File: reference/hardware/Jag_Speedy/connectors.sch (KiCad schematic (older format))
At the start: 8 parts, among them J1 Inputs, J2 Ouputs01, J3 Outputs02, J4 Power, J5 Bluetooth, J7 Canbus, U5 SN65HVD230

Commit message: Connector update
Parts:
- removed J1: Inputs, Connector_PinHeader_1.00mm:PinHeader_2x12_P1.00mm_Horizontal, symbol Connector_Generic:Conn_01x24
- removed J2: Ouputs01, Connector_PinHeader_1.00mm:PinHeader_2x07_P1.00mm_Horizontal, symbol Connector_Generic:Conn_01x14
- removed J3: Outputs02, Connector_PinHeader_1.00mm:PinHeader_2x05_P1.00mm_Horizontal, symbol Connector_Generic:Conn_01x10
- removed J4: Power, Connector_PinHeader_1.00mm:PinHeader_1x05_P1.00mm_Horizontal, symbol Connector_Generic:Conn_01x05
- removed J5: Bluetooth, Connector_PinHeader_1.00mm:PinHeader_1x06_P1.00mm_Horizontal, symbol Connector_Generic:Conn_01x06
- removed J7: Canbus, Connector_PinHeader_1.00mm:PinHeader_1x06_P1.00mm_Horizontal, symbol Connector_Generic:Conn_01x02
- added J1: 776087-1, 776087-1:7760871, symbol 776087-1:776087-1
- added J2: 776163-1, 776163-1:776163-1, symbol 776163-1:776163-1
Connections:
- net 12VRaw: now also J1.14
- net 3V3: now also J1.20, J2.1
- net 5V: now also J1.11, J1.19, J2.18
- net BluetoothRx: now also J1.22
- net BluetoothTx: now also J1.23
- net BoostPWM-OUT: now also J1.1
- net CCPump-OUT: now also J1.2
- net CLTSensor: now also J2.8
- net CamSensor+: now also J2.16
- net CamSensor-: now also J2.17
- net ClutchSwitch: now also J2.21
- net CrankSensor+: now also J2.14
- net CrankSensor-: now also J2.15
- net Fan-OUT: now also J1.5
- net FlexFuelSensor: now also J2.2
- net FuelPressureSensor: now also J2.19
- net FuelPump-OUT: now also J1.4
- net GND: now also J1.10, J1.17, J1.18, J1.21, J1.3, J1.9, J2.11, J2.12, J2.13, J2.22, J2.3, J2.35, J2.5, J2.7, J2.9
- net IATSensor: now also J2.6
- net Idle02-OUT: now also J1.7
- net IdlePWM-OUT: now also J1.6
- net Ign01-OUT: now also J2.29
- net Ign02-OUT: now also J2.30
- net Ign03-OUT: now also J2.31
- net Ign04-OUT: now also J2.32
- net Ign05-OUT: now also J2.33
- net Ign06-OUT: now also J2.34
- net Inj01-OUT: now also J2.23
- net Inj02-OUT: now also J2.24
- net Inj03-OUT: now also J2.25
- net Inj04-OUT: now also J2.26
- net Inj05-OUT: now also J2.27
- net Inj06-OUT: now also J2.28
- net O2Sensor: now also J2.10
- net OilPressureSensor: now also J2.20
- net TPSSensor: now also J2.4
- net Tacho-OUT: now also J1.8
- net CANL: now reaches U5.6 (CANL)
- net CANL: now also J1.16
- net CANH: now reaches U5.7 (CANH)
- net CANH: now also J1.15
- no-connect marks 3 -> 5
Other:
- moved on the sheet: R92, U5

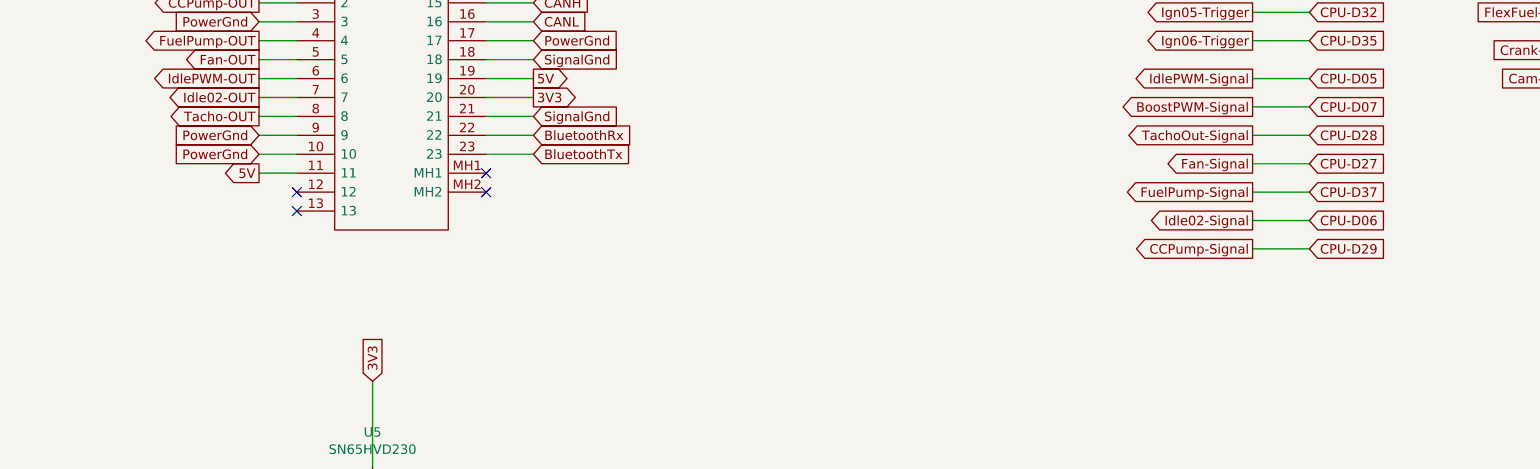
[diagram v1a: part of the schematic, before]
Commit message: Added Water Pump PWM
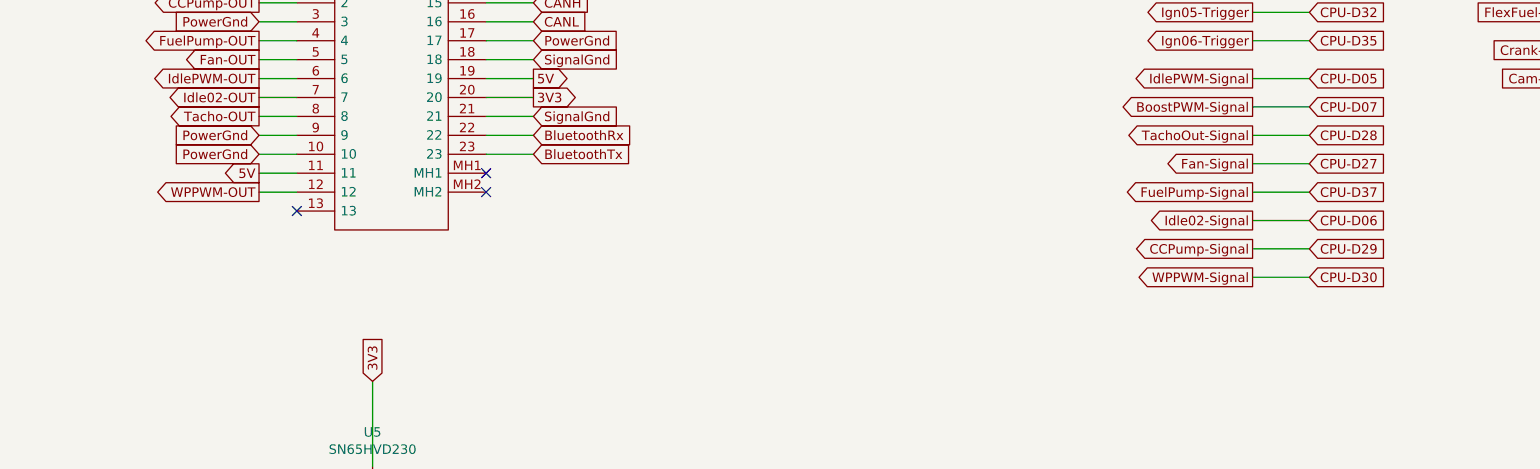
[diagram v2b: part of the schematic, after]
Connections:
- net WPPWM-OUT: now reaches J1.12
- no-connect marks 5 -> 4
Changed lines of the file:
@@
 	1750 4150 1950 4150
 NoConn ~ 1950 4350
-NoConn ~ 1950 4250
 NoConn ~ 2950 4250
 NoConn ~ 2950 4150
+Text GLabel 1750 4250 0    50   Output ~ 0
+WPPWM-OUT
+Wire Wire Line
+	1750 4250 1950 4250
+Text GLabel 7000 4700 0    50   Output ~ 0
+WPPWM-Signal
+Text GLabel 7300 4700 2    50   Input ~ 0
+CPU-D30
+Wire Wire Line
+	7300 4700 7000 4700
 $EndSCHEMATC

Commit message: EGR Input
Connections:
- net GND: no longer J2.12
- new net EGRSensor: J2.12
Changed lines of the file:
@@
 Wire Wire Line
 	2050 2050 1050 2050
-Wire Wire Line
-	1050 2050 1050 1950
 Text GLabel 3200 3650 2    50   Output ~ 0
 5V
@@
 Text GLabel 9250 2950 2    50   Output ~ 0
 CPU-A11
-Text GLabel 8800 3300 0    50   Input ~ 0
-FlexFuel-Signal
-Text GLabel 8800 3150 0    50   Input ~ 0
-ClutchIn-Signal
-Text GLabel 9250 3150 2    50   Output ~ 0
-CPU-D24
-Text GLabel 9250 3300 2    50   Output ~ 0
-CPU-D25
 Wire Wire Line
 	8800 1900 9250 1900
@@
 Wire Wire Line
 	9250 2950 8800 2950
-Wire Wire Line
-	8800 3150 9250 3150
-Wire Wire Line
-	9250 3300 8800 3300
 Text GLabel 8800 1750 0    50   Input ~ 0
 IAT-Signal-3V3
@@
 Wire Wire Line
 	8800 1750 9250 1750
-Text GLabel 8800 3500 0    50   Input ~ 0
-Crank-Signal
-Text GLabel 8800 3650 0    50   Input ~ 0
-Cam-Signal
-Text GLabel 9250 3650 2    50   Output ~ 0
-CPU-D36
-Text GLabel 9250 3500 2    50   Output ~ 0
-CPU-D23
-Wire Wire Line
-	8800 3650 9250 3650
-Wire Wire Line
-	9250 3500 8800 3500
 $Comp
 L Interface_CAN_LIN:SN65HVD230 U?
@@
 OilPressureSensor
 Wire Wire Line
-	2050 1950 1050 1950
-Connection ~ 1050 1950
-Wire Wire Line
-	1050 1950 1050 1850
-Wire Wire Line
 	3100 850  2950 850
 Wire Wire Line
@@
 Wire Wire Line
 	7300 4700 7000 4700
+Wire Wire Line
+	1050 1850 1050 2050
+Text GLabel 1900 1950 0    50   Input ~ 0
+EGRSensor
+Text GLabel 8800 3100 0    50   Input ~ 0
+EGR-Signal-3V3
+Text GLabel 9250 3100 2    50   Output ~ 0
+CPU-A6
+Wire Wire Line
+	9250 3100 8800 3100
+Wire Wire Line
+	9250 3700 8800 3700
+Wire Wire Line
+	8800 3850 9250 3850
+Text GLabel 9250 3700 2    50   Output ~ 0
+CPU-D23
+Text GLabel 9250 3850 2    50   Output ~ 0
+CPU-D36
+Text GLabel 8800 3850 0    50   Input ~ 0
+Cam-Signal
+Text GLabel 8800 3700 0    50   Input ~ 0
+Crank-Signal
+Wire Wire Line
+	9250 3500 8800 3500
+Wire Wire Line
+	8800 3350 9250 3350
+Text GLabel 9250 3500 2    50   Output ~ 0
+CPU-D25
+Text GLabel 9250 3350 2    50   Output ~ 0
+CPU-D24
+Text GLabel 8800 3350 0    50   Input ~ 0
+ClutchIn-Signal
+Text GLabel 8800 3500 0    50   Input ~ 0
+FlexFuel-Signal
+Wire Wire Line
+	2050 1950 1900 1950
 $EndSCHEMATC
